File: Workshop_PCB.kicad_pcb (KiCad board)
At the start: 2 copper layers, 23 parts, among them J1 Conn_01x04, J2 USB_C_Receptacle_USB2.0_16P, J3 Conn_01x22, J4 Conn_01x22, SW1 SW_Push, U1 STM32F042C6Tx, U2 AMS1117-3.3, U3 USBLC6-2SC6

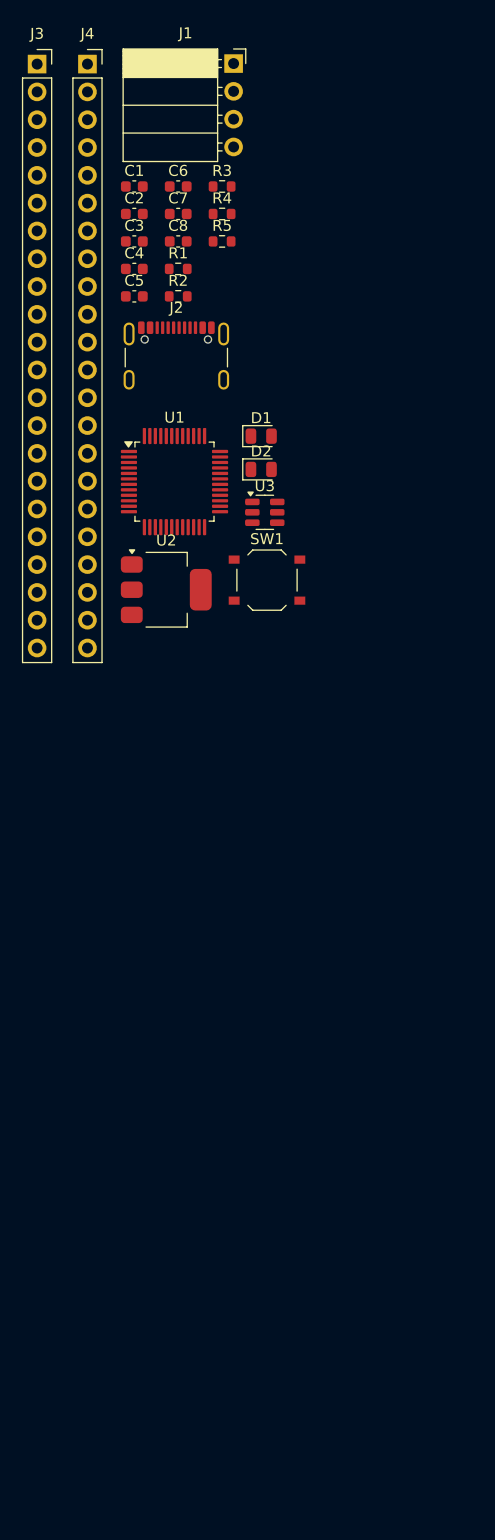
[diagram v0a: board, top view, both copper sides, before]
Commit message: Finish component selection and footprint assignment
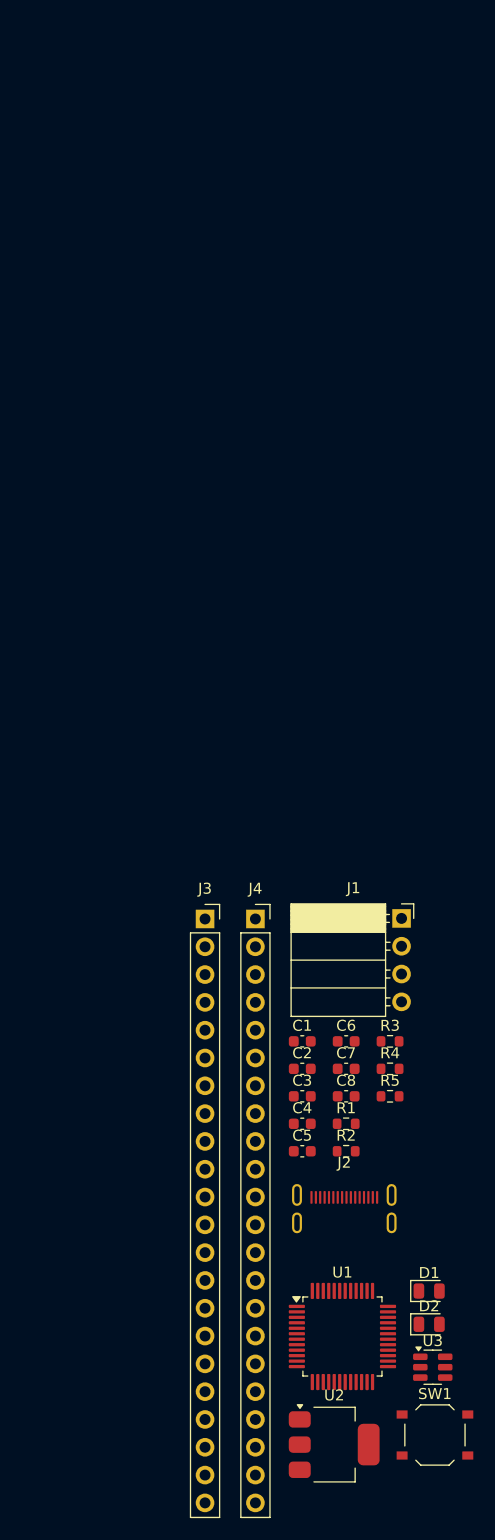
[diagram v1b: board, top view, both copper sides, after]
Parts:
- C8: value 20uF -> 22uF
- J2: footprint Connector_USB:USB_C_Receptacle_GCT_USB4105-xx-A_16P_TopMnt_Horizontal -> Connector_USB:USB_C_Receptacle_Hanbo_16P_TopMnt_Horizontal
- R2: value 220R -> 51R
- R5: value 50R -> 51R
- moved C4 79.6 mm to (93.9, 108.2)
- moved R1 79.6 mm to (98.0, 108.2)
- moved SW1 79.6 mm to (106.1, 136.7)
- moved U2 79.6 mm to (96.9, 137.5)
- moved C1 79.6 mm to (93.9, 100.7)
- moved C2 79.6 mm to (93.9, 103.2)
- moved C3 79.6 mm to (93.9, 105.7)
- moved C5 79.6 mm to (93.9, 110.7)
- moved C6 79.6 mm to (98.0, 100.7)
- moved C7 79.6 mm to (98.0, 103.2)
- moved C8 79.6 mm to (98.0, 105.7)
- moved D1 79.6 mm to (105.5, 123.5)
- moved D2 79.6 mm to (105.5, 126.6)
- moved J1 79.6 mm to (103.0, 89.5)
- moved J2 79.6 mm to (97.8, 117.3)
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
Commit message: Start tracing board
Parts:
- J1: footprint Connector_PinSocket_2.54mm:PinSocket_1x04_P2.54mm_Horizontal -> Connector_PinSocket_2.54mm:PinSocket_1x04_P2.54mm_Vertical
- moved C1 86.5 mm to (179.8, 110.7), turned to 180 degrees
- moved J1 81.4 mm to (184.2, 96.5)
- moved R1 77.1 mm to (175.0, 110.7)
- moved SW1 73.5 mm to (169.9, 100.3), turned to 90 degrees
- moved C3 71.7 mm to (165.1, 96.8), turned to -90 degrees
- moved C2 70.0 mm to (163.8, 106.4), turned to 180 degrees
- moved U1 67.2 mm to (159.0, 100.3)
- moved U2 61.9 mm to (146.3, 100.3), turned to -90 degrees
- moved C5 60.7 mm to (152.9, 96.5), turned to 90 degrees
- moved C4 58.5 mm to (152.1, 102.1), turned to 90 degrees
- moved C6 57.3 mm to (154.9, 95.0), turned to 90 degrees
- moved J3 51.4 mm to (130.6, 113.5), turned to 90 degrees
- moved C8 51.2 mm to (148.1, 95.0)
- moved D2 46.0 mm to (147.7, 108.2)
- moved U3 45.9 mm to (140.5, 100.3)
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- renumbered D1 to ON
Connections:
- U1 pad 10: A9 -> A0
- U1 pad 11: A8 -> A1
- U1 pad 12: A7 -> A2
- U1 pad 13: A6 -> A3
- U1 pad 14: A5 -> A4
- U1 pad 15: A4 -> A5
- U1 pad 16: A3 -> A6
- U1 pad 17: A2 -> A7
- U1 pad 18: A1 -> A8
- U1 pad 19: A0 -> A9
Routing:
- net USB_DM_D0: track 0.00 -> 52.3 mm, vias 0 -> 2
- net USB_DP_D1: track 0.00 -> 47.4 mm, vias 0 -> 3
- net D2: track 0.00 -> 42.3 mm
- net I2C_SCL_PWM_D3: track 0.00 -> 40.7 mm
- net I2C_SDA_PWM_D4: track 0.00 -> 39.0 mm
- net D7: track 0.00 -> 37.1 mm
- net D8: track 0.00 -> 37.0 mm
- net NRST: track 0.00 -> 36.2 mm, vias 0 -> 3
- net D5: track 0.00 -> 35.3 mm
- net D6: track 0.00 -> 34.6 mm
- net D20: track 0.00 -> 34.3 mm
- net BOOT: track 0.00 -> 32.5 mm, vias 0 -> 2
- net /SWCLK: track 0.00 -> 32.1 mm, vias 0 -> 1
- net CAN_TX_PWM_D19: track 0.00 -> 31.7 mm
- net D21: track 0.00 -> 30.8 mm
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- added copper zone on B.Cu, net GND
- added copper zone on F.Cu, net GND
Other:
- board outline added: 57.7 x 30.5 mm

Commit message: Finish PCB
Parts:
- added G***: LOGO, Symbol:logo, F.Cu at (181.6, 97.0)
- added REF**: Fiducial_0.5mm_Mask1mm, Fiducial:Fiducial_0.5mm_Mask1mm, F.Cu at (185.7, 91.9)
- added REF**: MountingHole_2.2mm_M2, MountingHole:MountingHole_2.2mm_M2, F.Cu at (187.5, 114.3)
- added REF**: MountingHole_2.2mm_M2, MountingHole:MountingHole_2.2mm_M2, F.Cu at (187.5, 86.4)
- added REF**: MountingHole_2.2mm_M2, MountingHole:MountingHole_2.2mm_M2, F.Cu at (127.3, 114.3)
- added REF**: Fiducial_0.5mm_Mask1mm, Fiducial:Fiducial_0.5mm_Mask1mm, F.Cu at (131.3, 93.2)
- added REF**: Fiducial_0.5mm_Mask1mm, Fiducial:Fiducial_0.5mm_Mask1mm, F.Cu at (128.3, 108.5)
- added REF**: MountingHole_2.2mm_M2, MountingHole:MountingHole_2.2mm_M2, F.Cu at (127.3, 86.4)
- J1: footprint Connector_PinSocket_2.54mm:PinSocket_1x04_P2.54mm_Vertical -> Connector_PinHeader_2.54mm:PinHeader_1x04_P2.54mm_Vertical
- moved R1 9.18 mm to (183.9, 108.5), turned to 180 degrees
- moved C1 5.58 mm to (183.9, 106.9)
- moved R3 2.90 mm to (136.1, 96.5)
- moved J1 2.82 mm to (187.0, 96.5)
- moved U3 2.79 mm to (137.7, 100.3)
- moved C8 2.78 mm to (145.3, 95.0)
- moved J2 2.54 mm to (130.6, 100.3)
- moved C7 2.03 mm to (139.7, 96.0)
- moved U2 2.03 mm to (144.3, 100.3)
- moved R4 1.52 mm to (133.6, 106.7)
- renumbered ON to D1
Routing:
- net +3V3: track 29.4 -> 131.3 mm, vias 0 -> 8
- net +5V: track 23.2 -> 91.4 mm
- net NRST: track 36.2 -> 46.8 mm
- net BOOT: track 32.5 -> 40.9 mm
- net GND: track 16.4 -> 20.2 mm, vias 0 -> 16
- net /SWDIO: track 29.8 -> 32.6 mm
- net /SWCLK: track 32.1 -> 35.0 mm
- net USB_DP_D1: track 47.4 -> 50.2 mm
- net USB_DM_D0: track 52.3 -> 54.8 mm
- net Net-(J2-D+-PadA6): track 7.12 -> 6.11 mm
- net Net-(J2-CC1): track 4.65 -> 4.09 mm
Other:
- board size 57.7 x 30.5 mm -> 62.7 x 30.5 mm
- board text added: "3.3V"
- board text added: "5V"
- board text added: "A0"
- board text added: "A1"
- board text added: "A2"
- board text added: "A3"
- board text added: "A4"
- board text added: "A5"
- board text added: "A6"
- board text added: "A7"
- board text added: "A8"
- board text added: "A9"
- board text added: "BOOT"
- board text added: "D0"
- board text added: "D1"
- board text added: "D10"
- board text added: "D11"
- board text added: "D12"
- board text added: "D13"
- board text added: "D14"
- board text added: "D15"
- board text added: "D16"
- board text added: "D17"
- board text added: "D18"
- board text added: "D19"
- board text added: "D2"
- board text added: "D20"
- board text added: "D21"
- board text added: "D22"
- board text added: "D23"
- board text added: "D3"
- board text added: "D4"
- board text added: "D5"
- board text added: "D6"
- board text added: "D7"
- board text added: "D8"
- board text added: "D9"
- board text added: "GND"
- board text added: "Hackpill"
- board text added: "Made by"
- board text added: "RESET"
- board text added: "VIN"

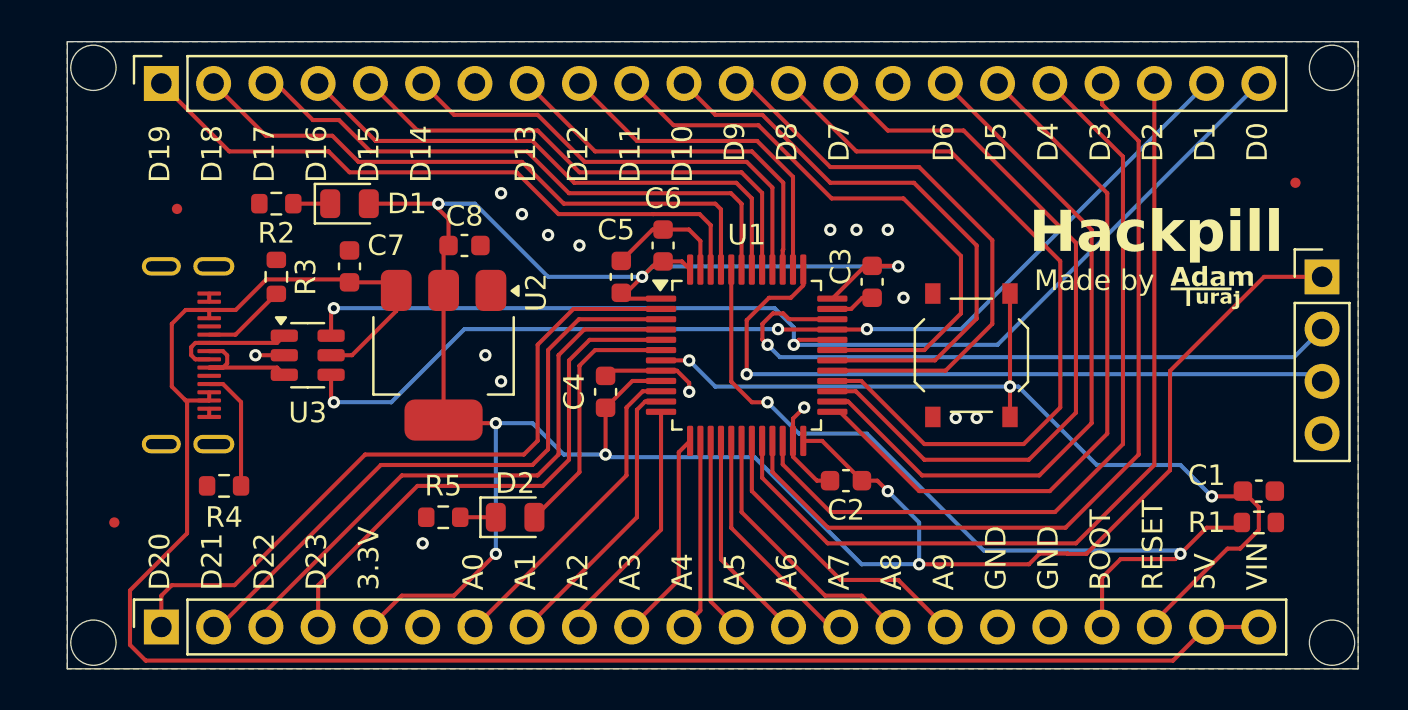
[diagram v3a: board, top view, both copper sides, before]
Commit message: Adjust trace width, adjust pinout, make changes to schematic
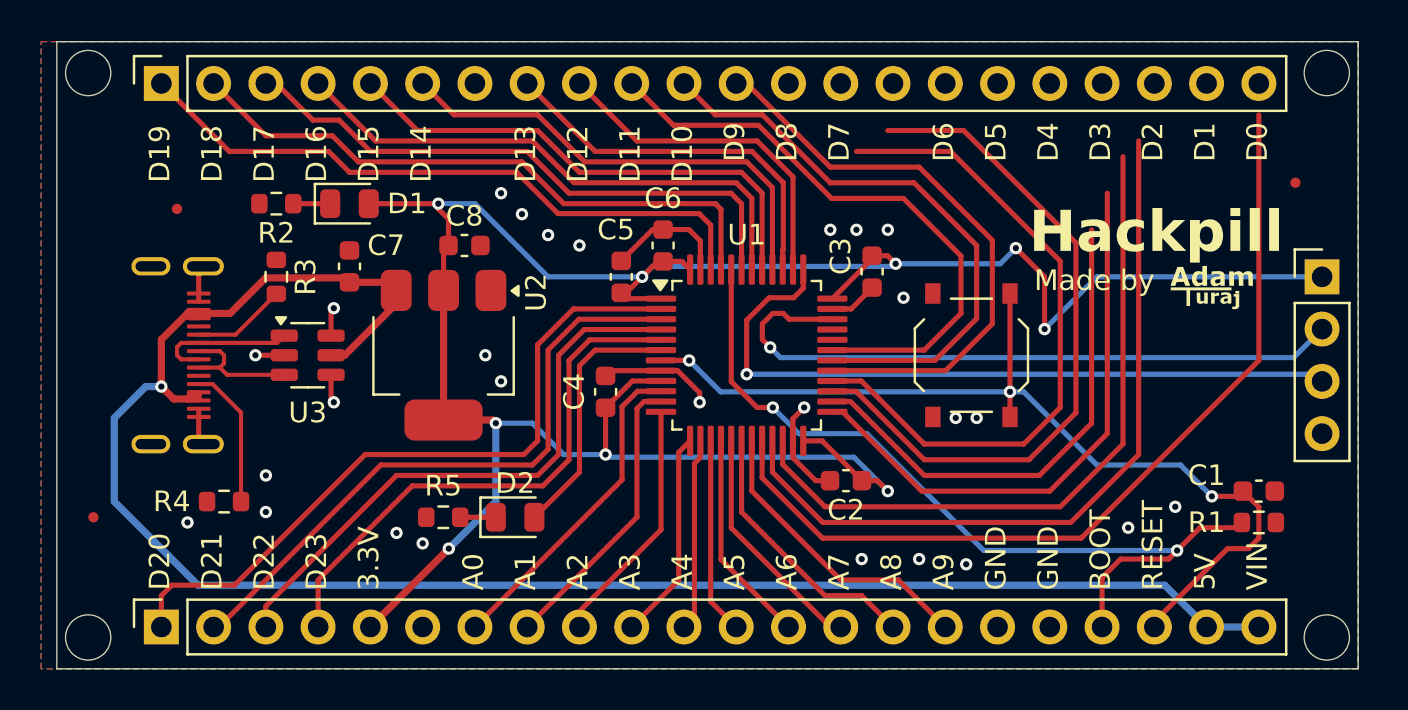
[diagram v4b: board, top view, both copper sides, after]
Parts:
- moved REF** 1.05 mm to (127.3, 108.2)
- moved R4 0.76 mm to (133.6, 107.4)
- moved J2 0.51 mm to (130.0, 100.3)
- moved C3 0.49 mm to (165.1, 96.3)
- moved REF** 0.36 mm to (127.0, 86.6)
- moved REF** 0.36 mm to (187.2, 86.6)
- moved REF** 0.36 mm to (127.0, 114.0)
- moved REF** 0.36 mm to (187.2, 114.0)
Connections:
- C7 pad 1: +5V -> Net-(U2-VI)
- J2 pad A4: +5V -> Net-(U2-VI)
- J2 pad A9: +5V -> Net-(U2-VI)
- J2 pad B4: +5V -> Net-(U2-VI)
- J2 pad B9: +5V -> Net-(U2-VI)
- J3 pad 1: D20 -> D18
- J3 pad 2: D21 -> D19
- J3 pad 3: D22 -> D20
- J3 pad 4: D23 -> D21
- J4 pad 1: CAN_TX_PWM_D19 -> unconnected-(J4-Pin_1-Pad1)
- J4 pad 10: USART_TX_PWM_D11 -> I2S_WS_PWM_D10
- J4 pad 11: USART_TX_PWM_D10 -> unconnected-(J4-Pin_11-Pad11)
- J4 pad 12: PWM_D9 -> USART_TX_PWM_D9
- J4 pad 13: D8 -> USART_TX_PWM_D8
- J4 pad 14: D7 -> PWM_D7
- J4 pad 15: unconnected-(J4-Pin_15-Pad15) -> D6
- J4 pad 16: D6 -> D5
- J4 pad 17: D5 -> unconnected-(J4-Pin_17-Pad17)
- J4 pad 18: I2C_SDA_PWM_D4 -> D4
- J4 pad 19: I2C_SCL_PWM_D3 -> D3
- J4 pad 2: CAN_RX_PWM_D18 -> CAN_TX_PWM_D17
- J4 pad 20: D2 -> I2C_SDA_PWM_D2
- J4 pad 21: USB_DP_D1 -> I2C_SCL_PWM_D1
- J4 pad 22: USB_DM_D0 -> D0
- J4 pad 3: D17 -> CAN_RX_PWM_D16
- J4 pad 4: D16 -> D15
- J4 pad 5: SPI_MOSI_I2S_SD_PWM_D15 -> unconnected-(J4-Pin_5-Pad5)
- J4 pad 6: SPI_MISO_I2S_MCK_PWM_D14 -> D14
- J4 pad 7: unconnected-(J4-Pin_7-Pad7) -> SPI_MOSI_I2S_SD_PWM_D13
- J4 pad 8: SPI_SCK_PWM_D13 -> SPI_MISO_I2S_MCK_PWM_D12
- J4 pad 9: I2S_WS_PWM_D12 -> SPI_SCK_PWM_D11
- U2 pad 3: +5V -> Net-(U2-VI)
- U3 pad 5: +5V -> Net-(U2-VI)
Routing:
- net USB_DM_D0: track 54.8 -> 1.39 mm, vias 2 -> 1
- net USB_DP_D1: track 50.2 -> 1.39 mm, vias 3 -> 1
- net +3V3: track 131.3 -> 120.1 mm, vias 8 -> 9
- net D6: track 34.6 -> 24.5 mm
- net D5: track 35.3 -> 27.8 mm
- net I2C_SDA_PWM_D4: track 39.0 -> 33.8 mm
- net D8: track 37.0 -> 32.3 mm
- net GND: track 20.2 -> 24.0 mm, vias 16 -> 25
- net I2C_SCL_PWM_D3: track 40.7 -> 36.9 mm
- net D7: track 37.1 -> 33.8 mm
- net +5V: track 91.4 -> 89.3 mm, vias 0 -> 1
- net Net-(J2-CC2): track 5.98 -> 7.23 mm
- net Net-(J2-D--PadA7): track 6.11 -> 6.97 mm
- net Net-(J2-CC1): track 4.09 -> 4.59 mm
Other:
- board size 62.7 x 30.5 mm -> 63.2 x 30.5 mm

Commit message: Complete fixes for PCB
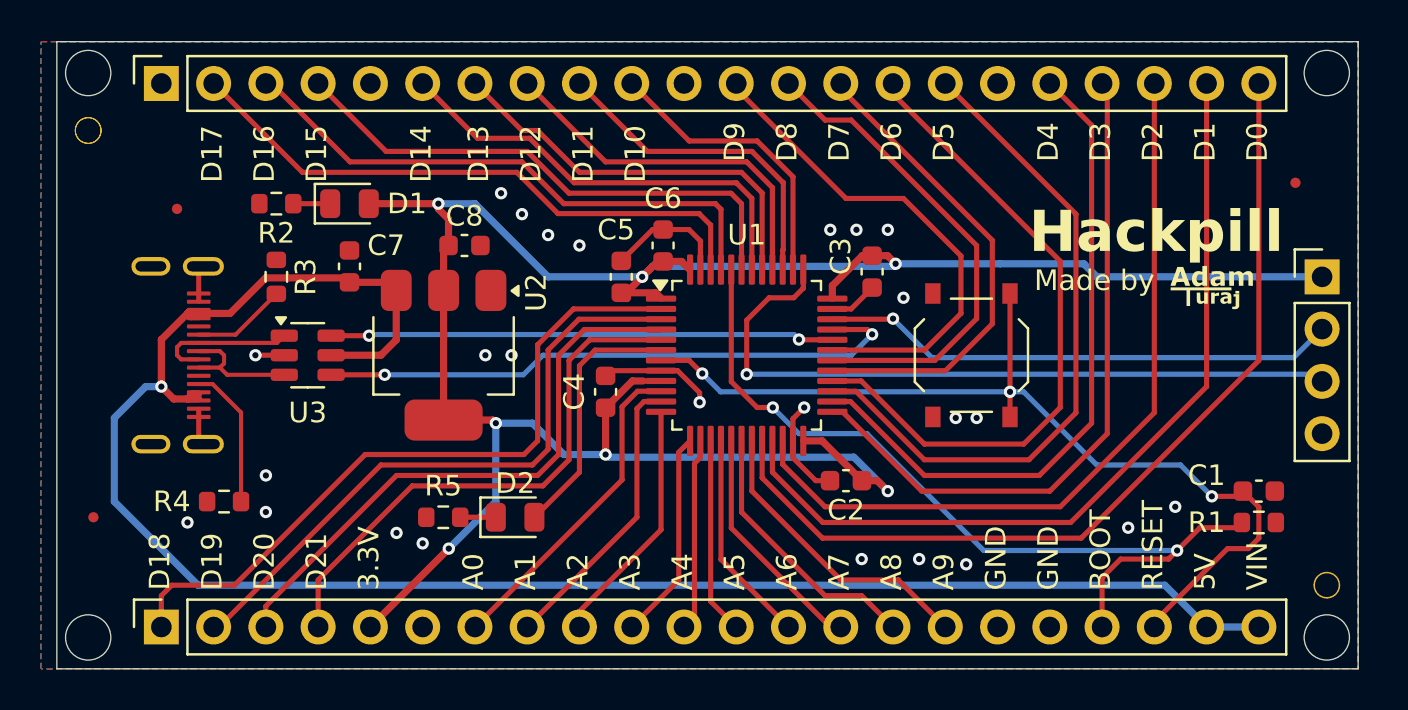
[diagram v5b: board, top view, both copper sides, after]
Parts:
- added ?: , , F.Cu at (127.0, 89.4)
- added REF**: Tooling_Hole_JLC, MountingHole:Tooling_Hole_JLC, F.Cu at (127.0, 89.4)
- added REF**: Tooling_Hole_JLC, MountingHole:Tooling_Hole_JLC, F.Cu at (187.2, 111.5)
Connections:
- net USB_DM_D0 renamed USB_DM
- net USB_DP_D1 renamed USB_DP
- C7 pad 1: Net-(U2-VI) -> +5V
- D2 pad 2: D24 -> D22
- J2 pad A4: Net-(U2-VI) -> +5V
- J2 pad A9: Net-(U2-VI) -> +5V
- J2 pad B4: Net-(U2-VI) -> +5V
- J2 pad B9: Net-(U2-VI) -> +5V
- U1 pad 2: D20 -> D18
- U1 pad 20: D2 -> D0
- U1 pad 21: I2C_SCL_PWM_D3 -> I2C_SCL_PWM_D1
- U1 pad 22: I2C_SDA_PWM_D4 -> I2C_SDA_PWM_D2
- U1 pad 25: D5 -> D3
- U1 pad 26: D6 -> D4
- U1 pad 27: D7 -> D5
- U1 pad 28: D8 -> D6
- U1 pad 29: PWM_D9 -> PWM_D7
- U1 pad 3: D21 -> D19
- U1 pad 30: USART_TX_PWM_D10 -> USART_TX_PWM_D8
- U1 pad 31: USART_TX_PWM_D11 -> USART_TX_PWM_D9
- U1 pad 38: I2S_WS_PWM_D12 -> I2S_WS_PWM_D10
- U1 pad 39: SPI_SCK_PWM_D13 -> SPI_SCK_PWM_D11
- U1 pad 4: D22 -> D20
- U1 pad 40: SPI_MISO_I2S_MCK_PWM_D14 -> SPI_MISO_I2S_MCK_PWM_D12
- U1 pad 41: SPI_MOSI_I2S_SD_PWM_D15 -> SPI_MOSI_I2S_SD_PWM_D13
- U1 pad 42: D16 -> D14
- U1 pad 43: D17 -> D15
- U1 pad 45: CAN_RX_PWM_D18 -> CAN_RX_PWM_D16
- U1 pad 46: CAN_TX_PWM_D19 -> CAN_TX_PWM_D17
- U1 pad 5: D23 -> D21
- U1 pad 6: D24 -> D22
- U2 pad 3: Net-(U2-VI) -> +5V
- U3 pad 5: Net-(U2-VI) -> +5V
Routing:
- net D0: track 0.00 -> 44.2 mm
- net D2: track 42.7 -> 0.00 mm
- net I2C_SCL_PWM_D1: track 0.00 -> 41.1 mm
- net I2C_SDA_PWM_D2: track 0.00 -> 38.0 mm
- net I2C_SCL_PWM_D3: track 36.9 -> 0.00 mm
- net D18: track 0.00 -> 34.3 mm
- net D7: track 33.8 -> 0.00 mm
- net I2C_SDA_PWM_D4: track 33.8 -> 0.00 mm
- net D3: track 0.00 -> 33.2 mm
- net D4: track 0.00 -> 32.5 mm
- net D8: track 32.3 -> 0.00 mm
- net CAN_TX_PWM_D19: track 31.7 -> 0.00 mm
- net D19: track 0.00 -> 30.8 mm
- net CAN_RX_PWM_D18: track 30.1 -> 0.00 mm
- net USART_TX_PWM_D11: track 29.3 -> 0.00 mm
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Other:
- board text removed: "D22"
- board text removed: "D23"
